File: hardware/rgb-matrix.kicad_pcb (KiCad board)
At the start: 4 copper layers, 58 x 58 mm, 80 parts, among them CON1 VEXT, P1 MATRIX_BOT, P10 PSOUTH, P11 PEAST, P12 WEST, P13 NORTH, P14 SOUTH, P15 EAST, P2 MATRIX_TOP, P3 SWD, P4 SPI3, P5 UART5, P6 VEXT, P7 USB_B, P8 PWEST, P9 PNORTH, SW1 RESET, SW2 BOOT, U1 74AC244, U2 74AC244, U3 74AC244, U4 ULN2803A, U5 STM32F405R, U6 LD3985M33R, U7 USBUFxxW6, X1 8MHz

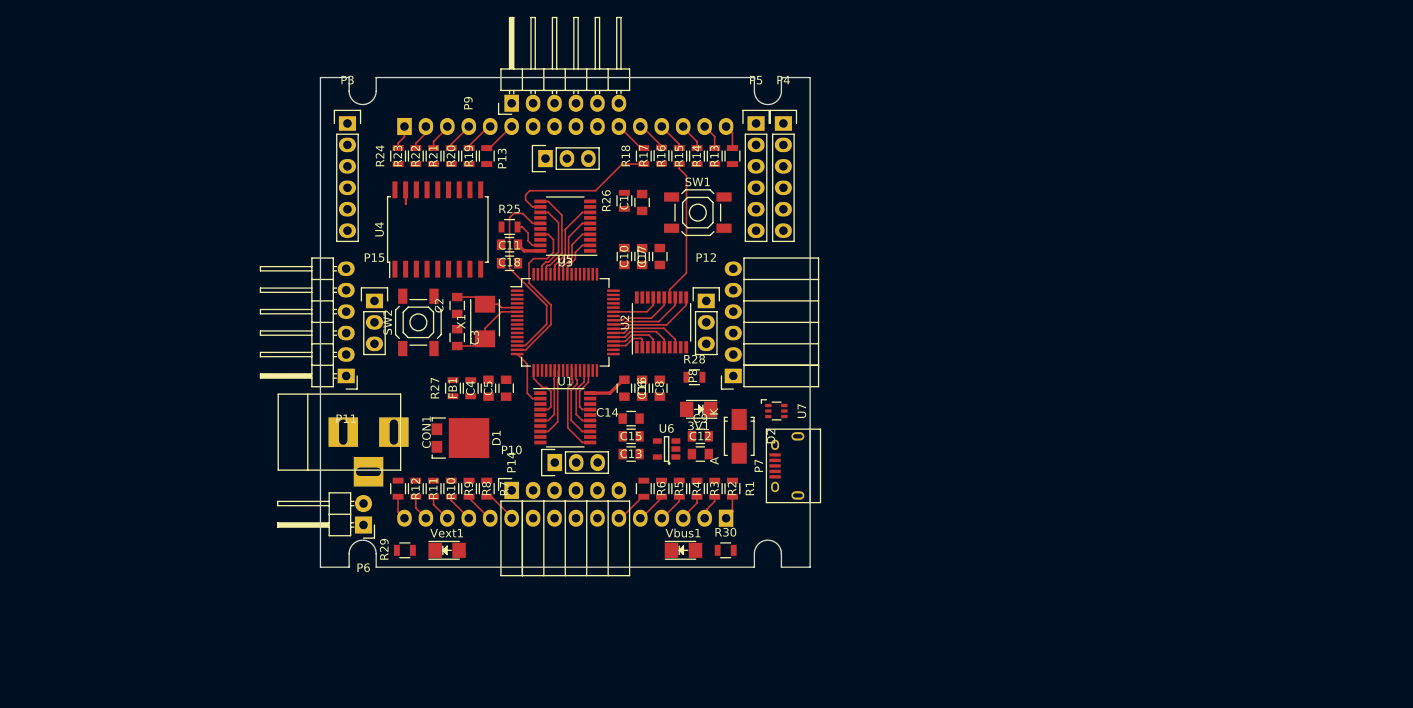
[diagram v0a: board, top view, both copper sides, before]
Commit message: Fix IRF7324 footprint
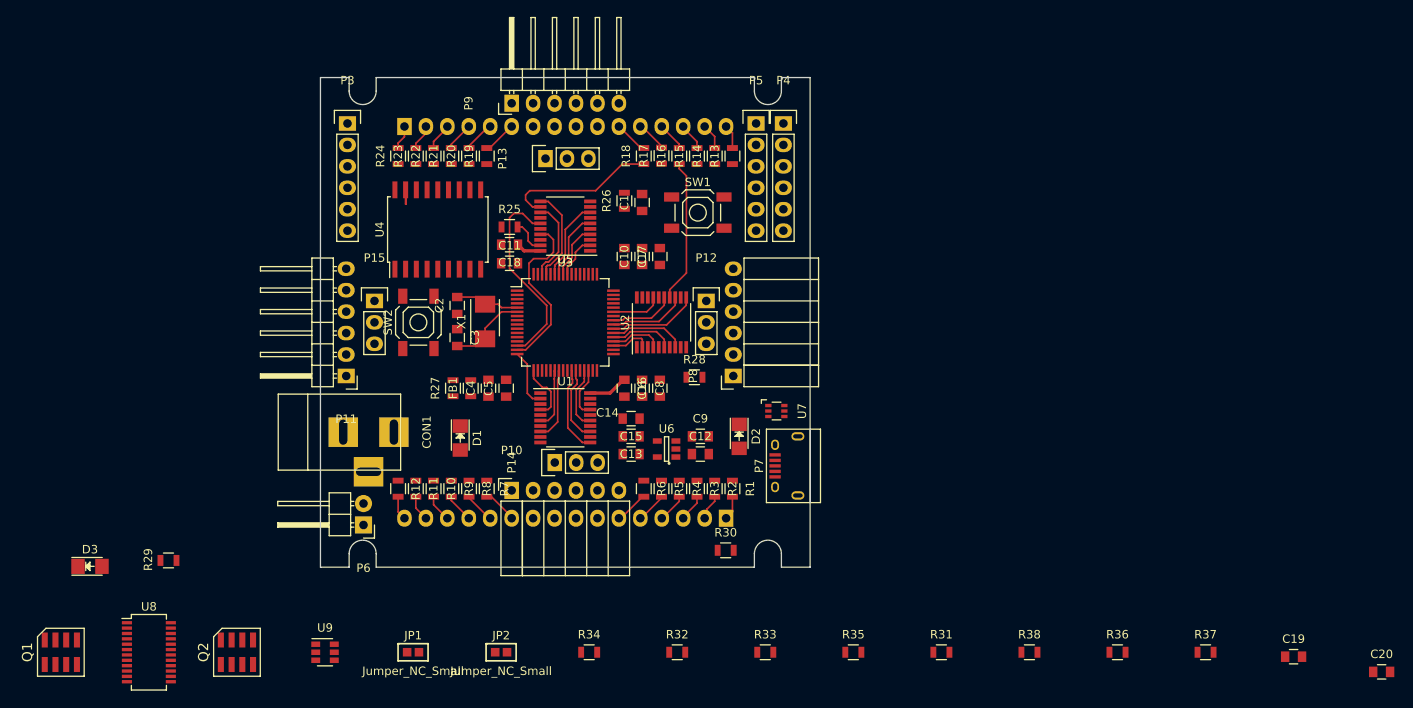
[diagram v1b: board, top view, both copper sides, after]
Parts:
- removed 3V1, Vbus1, Vext1: LED, LEDs:LED_1206
- added C19: 10uF, Capacitors_SMD:C_0805, F.Cu at (248.4, 140.8)
- added C20: 10uF, Capacitors_SMD:C_0805, F.Cu at (258.9, 142.6)
- added D3: Vbus, LEDs:LED_1206, F.Cu at (105.9, 130.1)
- added JP1: Jumper_NC_Small, KiCad-Footprints:MADW__SMD-solder-bridge, F.Cu at (144.1, 140.3)
- added JP2: Jumper_NC_Small, KiCad-Footprints:MADW__SMD-solder-bridge, F.Cu at (154.6, 140.3)
- added Q1: IRF7324PBF, rgb-matrix:SOIC-8, F.Cu at (102.4, 140.3)
- added Q2: IRF7324PBF, rgb-matrix:SOIC-8, F.Cu at (123.3, 140.3)
- added R31: 1M, Resistors_SMD:R_0805, F.Cu at (206.7, 140.3)
- added R32: 1M, Resistors_SMD:R_0805, F.Cu at (175.4, 140.3)
- added R33: 412k, Resistors_SMD:R_0805, F.Cu at (185.9, 140.3)
- added R34: 33.2k, Resistors_SMD:R_0805, F.Cu at (165.0, 140.3)
- added R35: 100k, Resistors_SMD:R_0805, F.Cu at (196.3, 140.3)
- added R36: 412k, Resistors_SMD:R_0805, F.Cu at (227.6, 140.3)
- added R37: 37.4k, Resistors_SMD:R_0805, F.Cu at (238.0, 140.3)
- added R38: 95.3k, Resistors_SMD:R_0805, F.Cu at (217.1, 140.3)
- added U8: LTC4417, Housings_SSOP:SSOP-24_3.9x8.7mm_Pitch0.635mm, F.Cu at (112.8, 140.3)
- added U9: 74x2G04, TO_SOT_Packages_SMD:SOT-23-6, F.Cu at (133.7, 140.3)
- D1: value FSV1045V -> 3.3V; footprint rgb-matrix:DIODE-TO-277A -> LEDs:LED_1206
- D2: value CDBA340L -> Vext; footprint Diodes_SMD:SMA_Standard -> LEDs:LED_1206
- moved R29 28.0 mm to (115.2, 129.4)
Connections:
- D1 pad 1: +5V -> GND
- D1 pad 2: /power/VEXT -> Net-(D1-Pad2)
- D2 pad 1: +5V -> GND
- D2 pad 2: VBUS -> Net-(D2-Pad2)
- R28 pad 2: Net-(3V1-Pad2) -> Net-(D1-Pad2)
- R29 pad 1: /power/VEXT -> Net-(R29-Pad1)
- R29 pad 2: Net-(R29-Pad2) -> Net-(D2-Pad2)
- R30 pad 1: VBUS -> Net-(R30-Pad1)
- U4 pad 9: GND -> Net-(JP1-Pad1)

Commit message: Preliminary routing with LTC4417
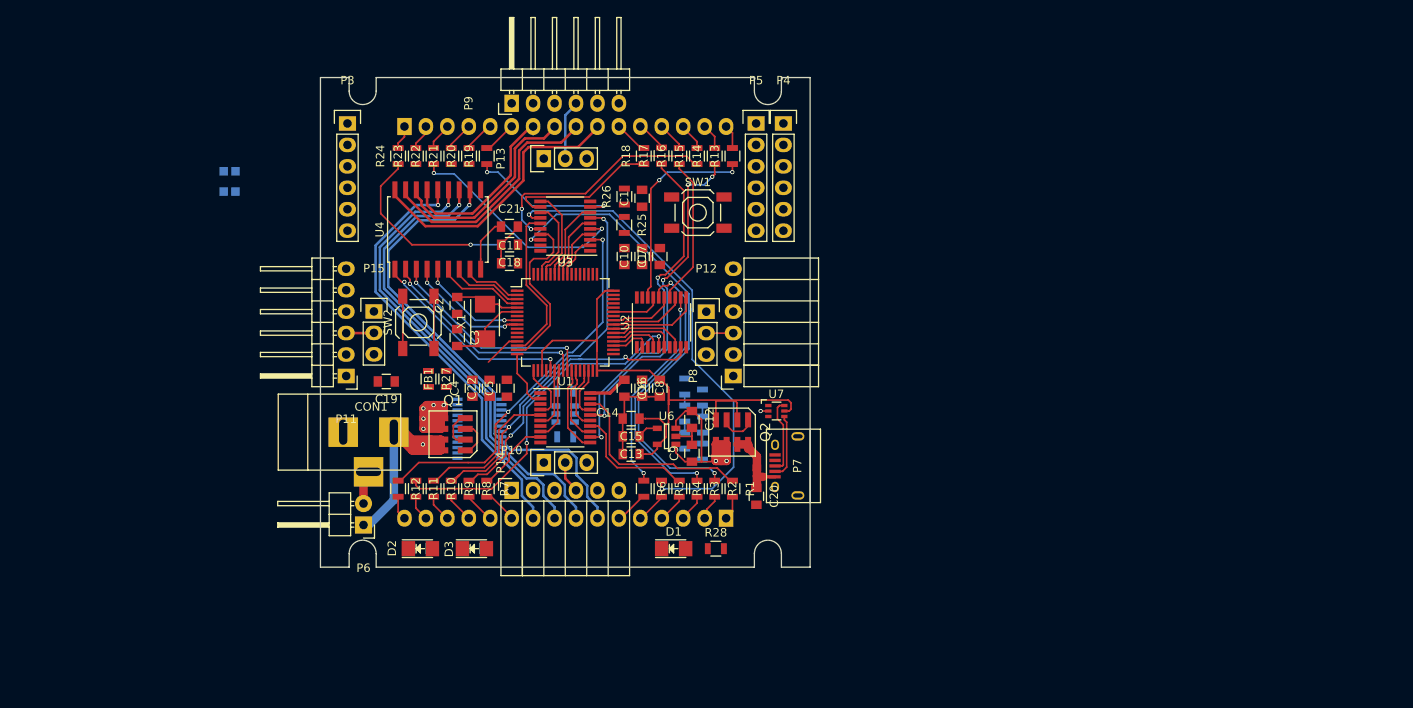
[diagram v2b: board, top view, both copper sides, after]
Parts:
- added C21: 100n, Capacitors_SMD:C_0805, F.Cu at (155.6, 89.8)
- added C22: 100nF, Capacitors_SMD:C_0805, F.Cu at (153.2, 109.0)
- JP1: value Jumper_NC_Small -> CA; moved to B.Cu
- JP2: value Jumper_NC_Small -> CC; moved to B.Cu
- R29, R30, R31, R32, R33, R34, R35, R36, R37, R38, U8, U9: moved to B.Cu
- moved C19 112.3 mm to (141.0, 108.2), turned to 180 degrees
- moved C20 76.9 mm to (184.8, 121.8), turned to 270 degrees
- moved R37 67.9 mm to (176.3, 112.0), turned to 270 degrees
- moved JP2 65.4 mm to (122.4, 83.3), turned to 180 degrees
- moved Q2 64.2 mm to (181.9, 114.2), turned to 180 degrees
- moved R36 60.2 mm to (176.3, 108.8), turned to 270 degrees
- moved JP1 58.7 mm to (122.4, 85.7)
- moved R31 54.2 mm to (162.2, 109.3)
- moved Q1 53.1 mm to (148.9, 114.4), turned to 90 degrees
- moved R38 47.9 mm to (176.3, 115.2), turned to 270 degrees
- moved U8 47.3 mm to (152.0, 113.8), turned to 180 degrees
- moved D3 45.6 mm to (151.4, 128.0)
- moved U9 40.1 mm to (162.2, 112.0), turned to 180 degrees
- moved D2 40.0 mm to (145.0, 128.0), turned to 0 degrees
- moved R33 31.1 mm to (178.4, 110.1), turned to 270 degrees
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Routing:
- net +3V3: track 0.00 -> 69.1 mm
- net ROW8: track 0.00 -> 59.8 mm, vias 0 -> 1
- net B3: track 0.00 -> 58.5 mm, vias 0 -> 2
- net ROW7: track 0.00 -> 56.8 mm, vias 0 -> 1
- net B1: track 0.00 -> 56.2 mm, vias 0 -> 2
- net ROW6: track 0.00 -> 54.2 mm, vias 0 -> 1
- net ROW5: track 0.00 -> 51.4 mm, vias 0 -> 1
- net +5V: track 7.96 -> 55.1 mm, vias 0 -> 7
- net B8: track 0.00 -> 45.4 mm, vias 0 -> 2
- net B6: track 0.00 -> 45.0 mm, vias 0 -> 2
- net G7: track 0.00 -> 42.0 mm, vias 0 -> 2
- net R4: track 0.00 -> 41.2 mm, vias 0 -> 2
- net R2: track 0.00 -> 39.9 mm, vias 0 -> 4
- net /power/VEXT: track 0.00 -> 37.4 mm, vias 0 -> 1
- net G5: track 0.00 -> 35.0 mm, vias 0 -> 2
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- added copper zone on 5V, net +5V
- added copper zone on GND, net GND
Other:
- net class +5V removed
- net class Default: via_dia 0.6 -> 0.5; via_drill 0.4 -> 0.3
- net class Power removed
- net class Vbus removed
- net class Vext removed
- rule trace_min: 0.2 -> 0.1524
- rule via_min_drill: 0.3 -> 0.254
- rule via_min_size: 0.4 -> 0.4572

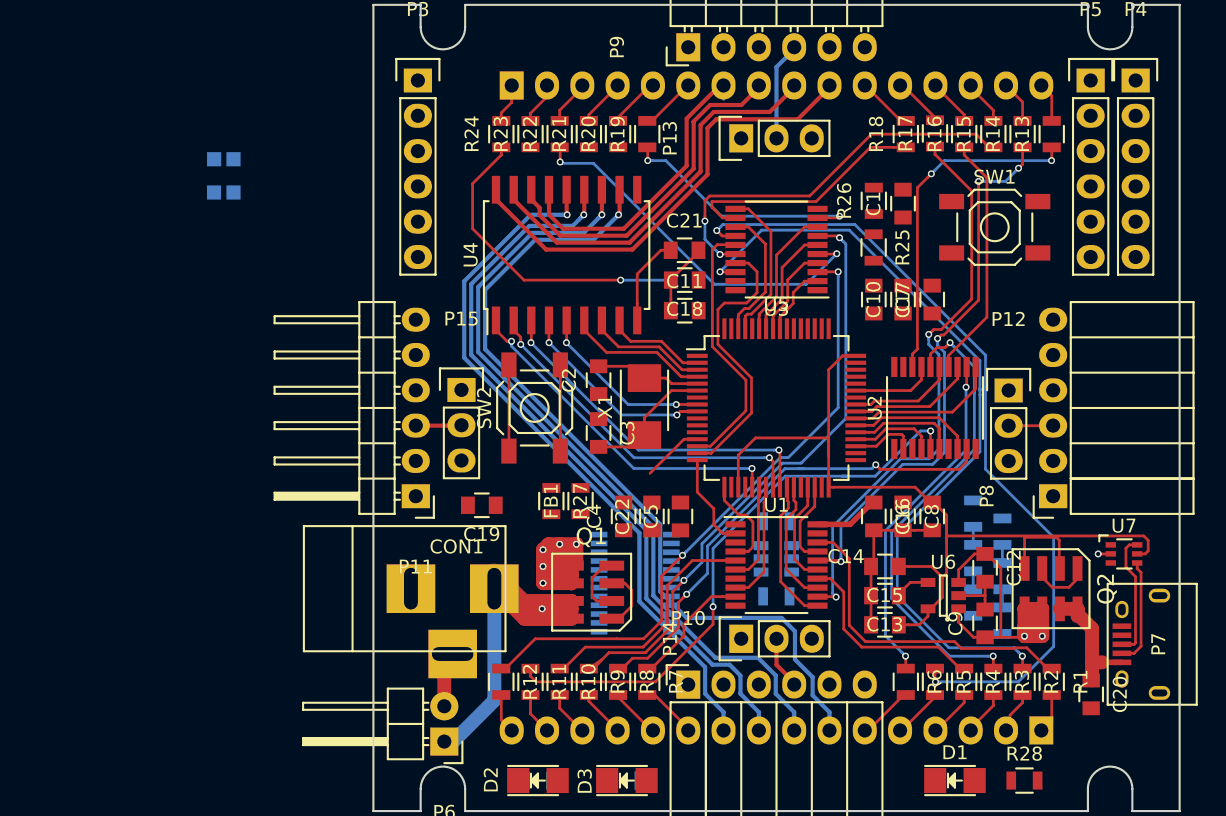
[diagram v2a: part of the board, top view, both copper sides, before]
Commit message: Probably not enough space for LTC4417
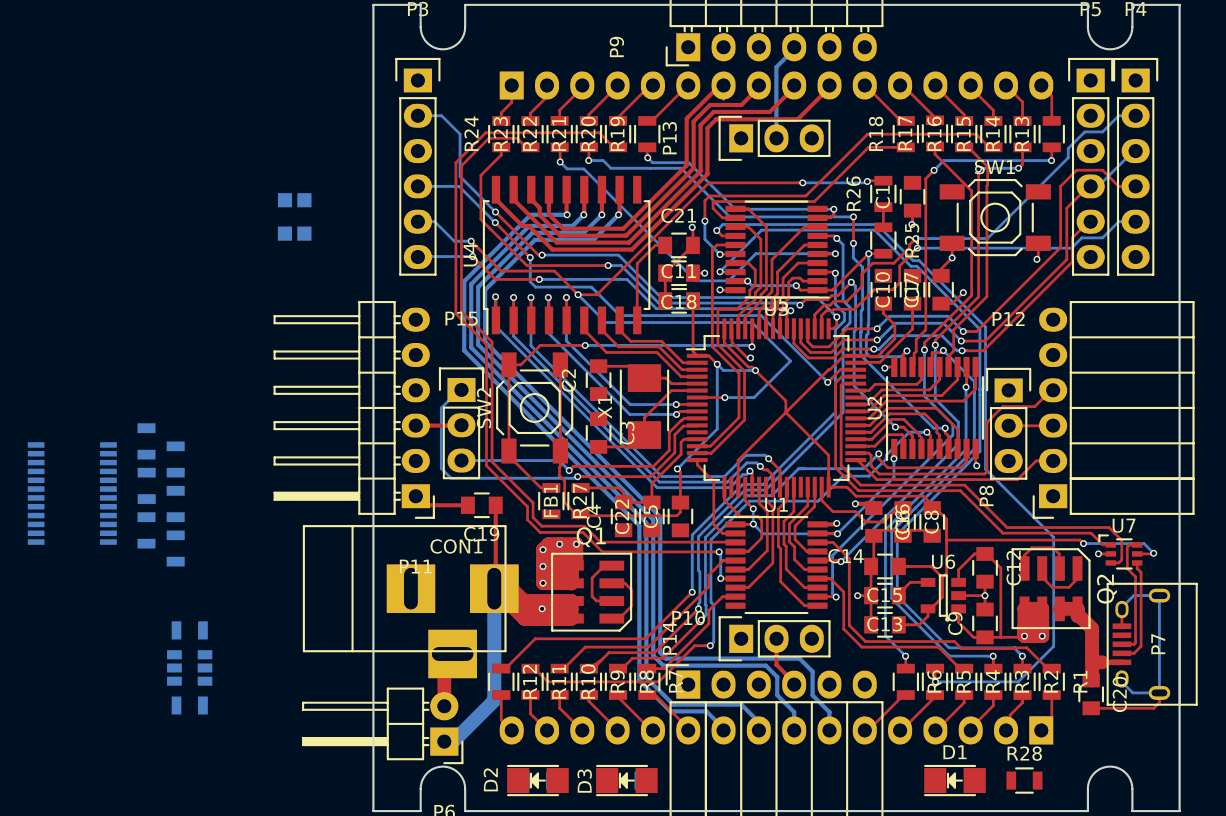
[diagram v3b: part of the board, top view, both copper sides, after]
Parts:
- moved R35 62.9 mm to (116.8, 103.6), turned to 90 degrees
- moved R34 61.9 mm to (116.8, 106.8), turned to 90 degrees
- moved R33 61.6 mm to (116.8, 110.0), turned to 90 degrees
- moved R38 58.3 mm to (118.9, 104.9), turned to 90 degrees
- moved R37 57.5 mm to (118.9, 108.1), turned to 90 degrees
- moved R36 57.4 mm to (118.9, 111.3), turned to 90 degrees
- moved R31 42.9 mm to (120.0, 117.2)
- moved R32 42.9 mm to (120.0, 122.6)
- moved U9 42.9 mm to (120.0, 119.9)
- moved U8 41.0 mm to (111.5, 107.3)
- moved JP1 5.89 mm to (127.5, 88.7)
- moved JP2 5.89 mm to (127.5, 86.2)
- moved C7 0.98 mm to (169.8, 92.7)
- moved C10 0.98 mm to (171.9, 92.7)
- moved C17 0.95 mm to (174.0, 92.7)
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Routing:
- net /mcu/NRST: track 0.00 -> 64.3 mm, vias 0 -> 5
- net R6: track 0.00 -> 58.6 mm, vias 0 -> 2
- net R8: track 0.00 -> 48.8 mm
- net +3V3: track 69.1 -> 116.9 mm, vias 0 -> 5
- net OE: track 0.00 -> 43.8 mm, vias 0 -> 8
- net G6: track 0.00 -> 41.9 mm, vias 0 -> 4
- net /mcu/JTCK/SWCLK: track 0.00 -> 39.2 mm, vias 0 -> 3
- net /mcu/JTMS/SWDIO: track 0.00 -> 38.7 mm, vias 0 -> 3
- net GND: track 25.1 -> 60.5 mm, vias 1 -> 9
- net /mcu/SPI3_MOSI: track 0.00 -> 34.6 mm, vias 0 -> 2
- net /mcu/SPI3_MISO: track 0.00 -> 33.9 mm, vias 0 -> 2
- net /mcu/USB_DM: track 0.00 -> 31.6 mm
- net /mcu/SPI3_SCK: track 0.00 -> 31.0 mm, vias 0 -> 1
- net /mcu/SWO: track 0.00 -> 29.9 mm, vias 0 -> 3
- net /mcu/USB_DP: track 0.00 -> 29.8 mm
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
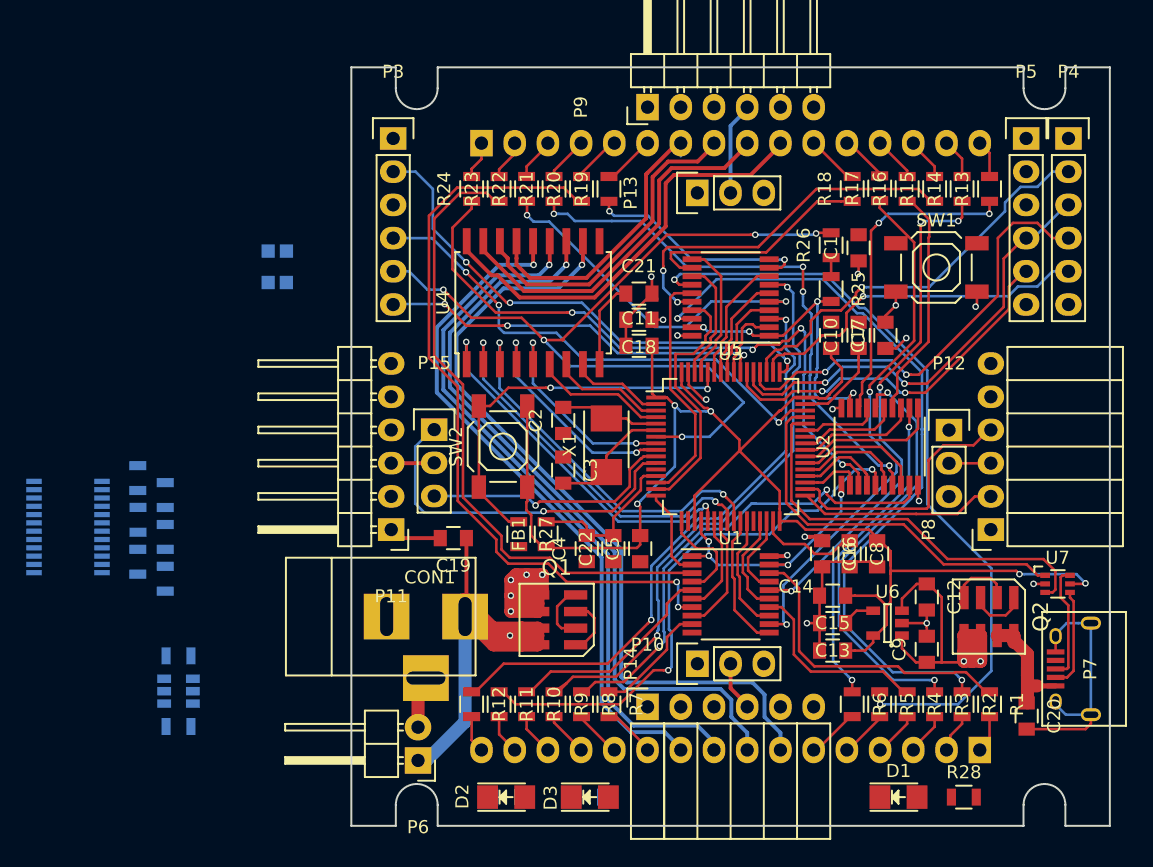
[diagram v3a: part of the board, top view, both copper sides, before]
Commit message: Completely routed PCB!
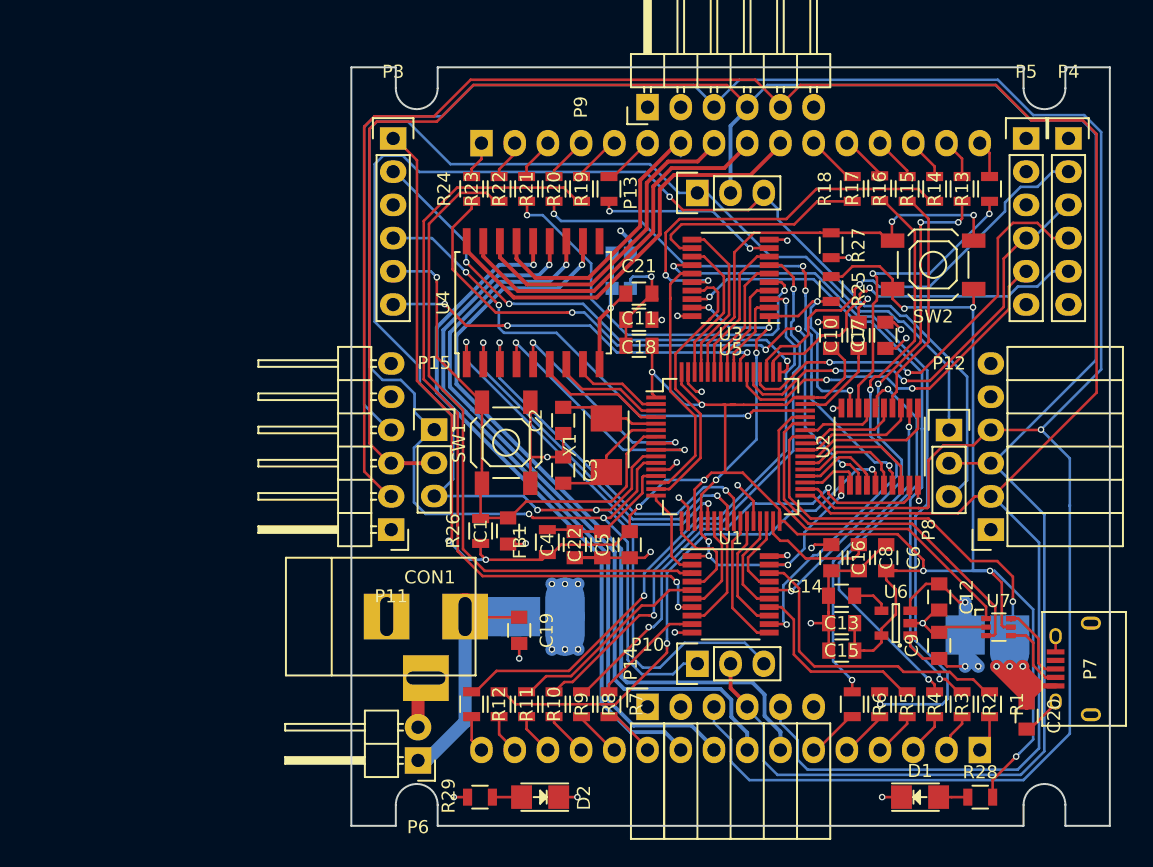
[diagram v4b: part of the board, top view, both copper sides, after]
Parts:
- removed D3: Vbus, LEDs:LED_1206
- removed Q1, Q2: IRF7324PBF, rgb-matrix:SOIC-8
- removed R30: 1k, Resistors_SMD:R_0805
- removed R31, R32: 1M, Resistors_SMD:R_0805
- removed R33, R36: 412k, Resistors_SMD:R_0805
- removed R34: 33.2k, Resistors_SMD:R_0805
- removed R35: 100k, Resistors_SMD:R_0805
- removed R37: 37.4k, Resistors_SMD:R_0805
- removed R38: 95.3k, Resistors_SMD:R_0805
- removed U8: LTC4417, Housings_SSOP:SSOP-24_3.9x8.7mm_Pitch0.635mm
- removed U9: 74x2G04, TO_SOT_Packages_SMD:SOT-23-6
- added JP3: Vext, rgb-matrix:SMD-solder-bridge-3mm, B.Cu at (147.8, 114.2)
- added JP4: Vbus, rgb-matrix:SMD-solder-bridge-3mm, B.Cu at (181.8, 115.6)
- D2: value Vext -> 5V
- JP1, JP2: footprint KiCad-Footprints:MADW__SMD-solder-bridge -> rgb-matrix:SMD-solder-bridge-1mm
- R29: moved to F.Cu
- moved SW2 35.7 mm to (177.7, 87.3), turned to 0 degrees
- moved SW1 35.5 mm to (145.0, 100.9), turned to 90 degrees
- moved R26 34.6 mm to (143.1, 107.7)
- moved C1 34.5 mm to (145.2, 107.7)
- moved R27 32.5 mm to (169.8, 85.8)
- moved JP2 26.5 mm to (153.8, 89.1)
- moved JP1 26.4 mm to (153.8, 86.4)
- moved C19 8.67 mm to (146.0, 115.2), turned to 270 degrees
- moved U7 5.59 mm to (182.7, 115.0)
- moved D2 2.60 mm to (147.6, 128.0), turned to 180 degrees
- moved C15 2.21 mm to (170.7, 114.7)
- moved C13 2.21 mm to (170.7, 112.6)
- moved R29 2.00 mm to (143.0, 128.0)
- moved D1 1.65 mm to (176.7, 128.0)
- moved U3 1.50 mm to (162.2, 88.3)
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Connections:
- R29 pad 1: Net-(R29-Pad1) -> +5V
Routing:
- net SPI2_SCK: track 19.8 -> 190.0 mm, vias 0 -> 1
- net /daisy/DATA: track 17.7 -> 183.7 mm
- net SPI2_NSS: track 15.3 -> 181.2 mm
- net SPI2_MISO: track 19.6 -> 137.6 mm, vias 1 -> 3
- net SPI2_MOSI: track 27.4 -> 128.7 mm, vias 1 -> 2
- net +3V3: track 116.9 -> 198.2 mm, vias 5 -> 11
- net VBUS: track 10.7 -> 49.4 mm, vias 0 -> 4
- net /mcu/NRST: track 64.3 -> 41.4 mm, vias 5 -> 1
- net GND: track 60.5 -> 82.3 mm, vias 9 -> 20
- net /power/VEXT: track 43.5 -> 23.5 mm, vias 1 -> 0
- net OE: track 43.8 -> 60.6 mm, vias 8 -> 10
- net +5V: track 57.8 -> 44.5 mm, vias 13 -> 17
- net B1: track 57.5 -> 48.2 mm
- net Net-(Q2-Pad2): track 5.08 -> 0.00 mm
- net Net-(Q1-Pad2): track 4.66 -> 0.00 mm
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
